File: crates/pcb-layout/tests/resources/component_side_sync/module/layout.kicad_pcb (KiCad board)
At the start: 2 copper layers, 2 parts

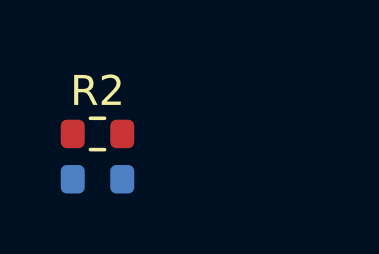
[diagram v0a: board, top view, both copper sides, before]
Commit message: Fix orientation syncing for back components
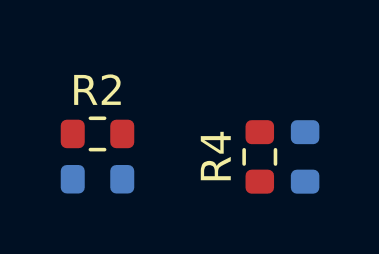
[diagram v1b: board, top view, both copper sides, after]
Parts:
- added R3: SMD 0603 1kOhms +/-10%, R_0603_1608Metric:R_0603_1608Metric, B.Cu at (155.4, 105.0)
- added R4: SMD 0603 1kOhms +/-10%, R_0603_1608Metric:R_0603_1608Metric, F.Cu at (153.9, 105.0)
- R1, R2: footprint Resistor_SMD:R_0603_1608Metric -> R_0603_1608Metric:R_0603_1608Metric
